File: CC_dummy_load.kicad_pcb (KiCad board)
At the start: 2 copper layers, 120 x 79.8 mm, 58 parts, among them P1 CONN_01X02, P2 12vFAN, P3 CONN_01X09, P4 LOAD, Q1 Darl_NPN, Q2 IRF540N, U1 LM324N, U2 MCP4921-E/P, U3 LM35

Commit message: redesign with much more vias to be able to make it DIY
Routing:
- net GND: track 49.2 -> 239.4 mm, vias 0 -> 4
- net VREF: track 100.1 -> 111.4 mm, vias 0 -> 2
- net Net-(ADC1-Pad2): track 53.0 -> 60.6 mm, vias 0 -> 1
- net ARDU-P08: track 36.0 -> 29.9 mm, vias 0 -> 2
- net ARDU-P07: track 26.0 -> 31.8 mm, vias 0 -> 2
- net Net-(ADC1-Pad8): track 72.4 -> 76.5 mm, vias 0 -> 2
- net ARDU-P09: track 53.6 -> 57.4 mm
- net ARDU-P11: track 43.3 -> 46.7 mm, vias 0 -> 2
- net Net-(C2-Pad1): track 18.9 -> 21.8 mm, vias 0 -> 2
- net ADC-VIN: track 69.8 -> 72.6 mm, vias 0 -> 1
- net Net-(RV2-Pad1): track 21.8 -> 23.0 mm, vias 0 -> 2
- net VCC: track 226.6 -> 227.2 mm, vias 0 -> 1
- net Net-(Q2-Pad1): track 43.1 -> 43.0 mm, vias 0 -> 1
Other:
- net class Default: via_dia 0.6 -> 1.2; via_drill 0.4 -> 0.6

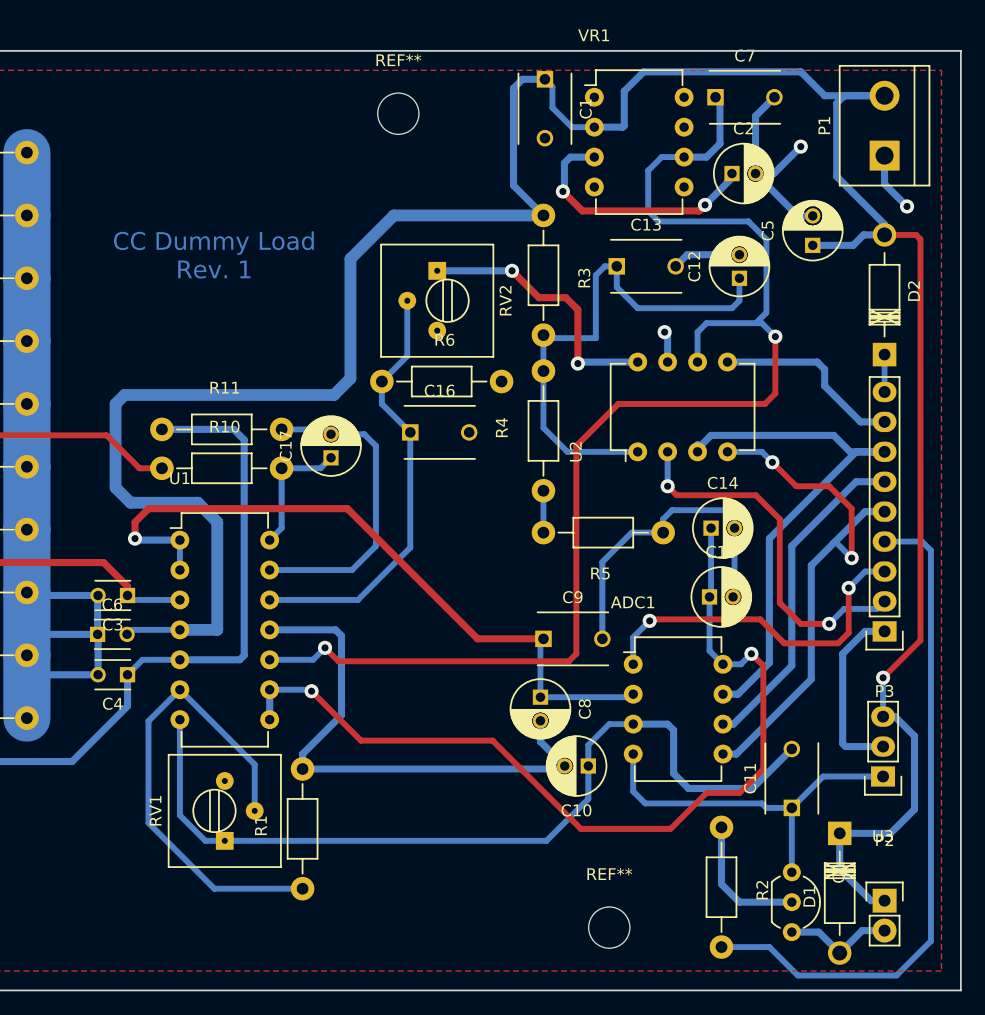
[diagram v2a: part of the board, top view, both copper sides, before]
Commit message: more coper on back face
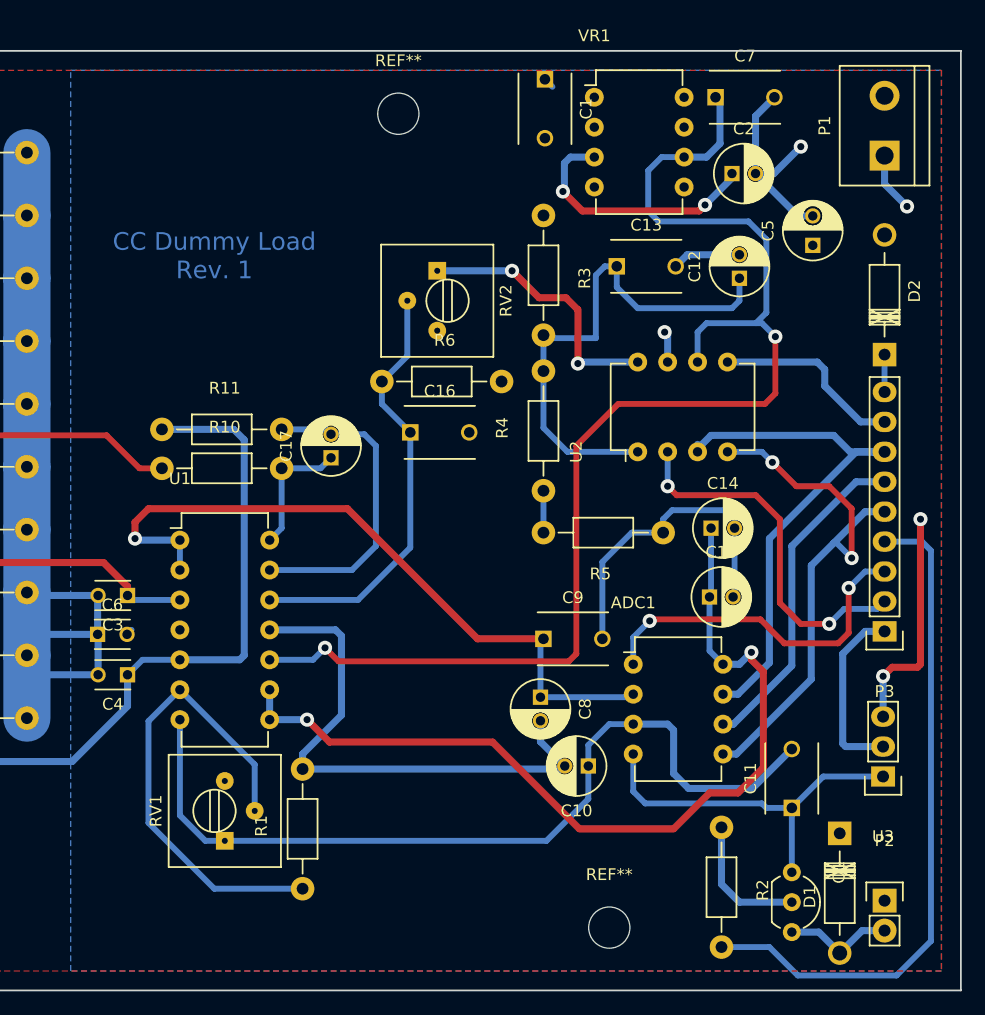
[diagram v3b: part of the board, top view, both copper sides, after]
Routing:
- net VCC: track 227.2 -> 20.8 mm, vias 1 -> 2
- net Net-(ADC1-Pad8): track 76.5 -> 75.6 mm
- added copper zone on B.Cu, net VCC
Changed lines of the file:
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@@
     (thickness 1.6)
     (drawings 6)
-    (tracks 410)
+    (tracks 365)
     (zones 0)
     (modules 58)
@@
   )
   (setup
-    (last_trace_width 0.5)
+    (last_trace_width 0.6)
     (user_trace_width 0.5)
     (user_trace_width 0.6)
@@
   (via (at 202.565 78.232) (size 1.2) (drill 0.6) (layers F.Cu B.Cu) (net 4))
   (segment (start 200.66 76.327) (end 202.565 78.232) (width 0.6) (layer B.Cu) (net 4))
-  (segment (start 182.927 83.312) (end 182.753 83.312) (width 0.5) (layer B.Cu) (net 4))
   (segment (start 187.928 111.252) (end 187.801 111.379) (width 0.5) (layer B.Cu) (net 4))
   (segment (start 173.26 125.984) (end 173.514 125.73) (width 0.6) (layer B.Cu) (net 4))
@@
   (segment (start 184.785 99.06) (end 184.785 98.425) (width 0.6) (layer B.Cu) (net 7))
   (segment (start 199.644 99.06) (end 200.66 99.06) (width 0.6) (layer B.Cu) (net 7))
-  (segment (start 148.463 119.253) (end 151.892 119.253) (width 0.5) (layer B.Cu) (net 8))
-  (segment (start 188.468 117.094) (end 186.944 117.094) (width 0.5) (layer B.Cu) (net 8))
-  (segment (start 189.357 116.205) (end 188.468 117.094) (width 0.5) (layer B.Cu) (net 8))
-  (via (at 189.357 116.205) (size 1.2) (drill 0.6) (layers F.Cu B.Cu) (net 8))
-  (segment (start 190.373 117.221) (end 189.357 116.205) (width 0.5) (layer F.Cu) (net 8))
-  (segment (start 190.373 125.984) (end 190.373 117.221) (width 0.5) (layer F.Cu) (net 8))
-  (segment (start 188.341 128.016) (end 190.373 125.984) (width 0.5) (layer F.Cu) (net 8))
-  (segment (start 185.547 128.016) (end 188.341 128.016) (width 0.5) (layer F.Cu) (net 8))
-  (segment (start 182.499 131.064) (end 185.547 128.016) (width 0.5) (layer F.Cu) (net 8))
-  (segment (start 174.879 131.064) (end 182.499 131.064) (width 0.5) (layer F.Cu) (net 8))
-  (segment (start 167.386 123.571) (end 174.879 131.064) (width 0.5) (layer F.Cu) (net 8))
-  (segment (start 156.21 123.571) (end 167.386 123.571) (width 0.5) (layer F.Cu) (net 8))
-  (segment (start 152.019 119.38) (end 156.21 123.571) (width 0.5) (layer F.Cu) (net 8))
-  (via (at 152.019 119.38) (size 1.2) (drill 0.6) (layers F.Cu B.Cu) (net 8))
-  (segment (start 151.892 119.253) (end 152.019 119.38) (width 0.5) (layer B.Cu) (net 8))
+  (segment (start 148.463 121.793) (end 151.638 121.793) (width 0.6) (layer B.Cu) (net 8))
+  (segment (start 188.341 117.094) (end 186.944 117.094) (width 0.6) (layer B.Cu) (net 8))
+  (segment (start 189.357 116.078) (end 188.341 117.094) (width 0.6) (layer B.Cu) (net 8))
+  (via (at 189.357 116.078) (size 1.2) (drill 0.6) (layers F.Cu B.Cu) (net 8))
+  (segment (start 189.357 116.713) (end 189.357 116.078) (width 0.6) (layer F.Cu) (net 8))
+  (segment (start 190.373 117.729) (end 189.357 116.713) (width 0.6) (layer F.Cu) (net 8))
+  (segment (start 190.373 125.857) (end 190.373 117.729) (width 0.6) (layer F.Cu) (net 8))
+  (segment (start 188.214 128.016) (end 190.373 125.857) (width 0.6) (layer F.Cu) (net 8))
+  (segment (start 185.801 128.016) (end 188.214 128.016) (width 0.6) (layer F.Cu) (net 8))
+  (segment (start 182.753 131.064) (end 185.801 128.016) (width 0.6) (layer F.Cu) (net 8))
+  (segment (start 174.752 131.064) (end 182.753 131.064) (width 0.6) (layer F.Cu) (net 8))
+  (segment (start 167.386 123.698) (end 174.752 131.064) (width 0.6) (layer F.Cu) (net 8))
+  (segment (start 153.543 123.698) (end 167.386 123.698) (width 0.6) (layer F.Cu) (net 8))
+  (segment (start 151.638 121.793) (end 153.543 123.698) (width 0.6) (layer F.Cu) (net 8))
+  (via (at 151.638 121.793) (size 1.2) (drill 0.6) (layers F.Cu B.Cu) (net 8))
   (segment (start 148.463 121.793) (end 148.463 119.253) (width 0.6) (layer B.Cu) (net 8))
   (segment (start 185.801 111.379) (end 185.801 115.951) (width 0.5) (layer B.Cu) (net 8))
@@
   (segment (start 185.928 105.537) (end 185.928 111.252) (width 0.5) (layer B.Cu) (net 8))
   (segment (start 185.928 111.252) (end 185.801 111.379) (width 0.5) (layer B.Cu) (net 8))
-  (segment (start 200.65746 80.645) (end 203.327 80.645) (width 0.5) (layer F.Cu) (net 9))
-  (segment (start 200.533 118.237) (end 200.533 121.539) (width 0.5) (layer B.Cu) (net 9))
-  (via (at 200.533 118.237) (size 1.2) (drill 0.6) (layers F.Cu B.Cu) (net 9))
-  (segment (start 203.708 115.062) (end 200.533 118.237) (width 0.5) (layer F.Cu) (net 9))
-  (segment (start 203.708 81.026) (end 203.708 115.062) (width 0.5) (layer F.Cu) (net 9))
-  (segment (start 203.327 80.645) (end 203.708 81.026) (width 0.5) (layer F.Cu) (net 9))
-  (segment (start 140.843 114.173) (end 144.018 114.173) (width 1) (layer B.Cu) (net 9))
-  (segment (start 159.004 78.994) (end 171.704 78.994) (width 1) (layer B.Cu) (net 9))
-  (segment (start 155.321 82.677) (end 159.004 78.994) (width 1) (layer B.Cu) (net 9))
-  (segment (start 155.321 92.837) (end 155.321 82.677) (width 1) (layer B.Cu) (net 9))
-  (segment (start 153.924 94.234) (end 155.321 92.837) (width 1) (layer B.Cu) (net 9))
-  (segment (start 136.144 94.234) (end 153.924 94.234) (width 1) (layer B.Cu) (net 9))
-  (segment (start 135.382 94.996) (end 136.144 94.234) (width 1) (layer B.Cu) (net 9))
-  (segment (start 135.382 102.108) (end 135.382 94.996) (width 1) (layer B.Cu) (net 9))
-  (segment (start 136.652 103.378) (end 135.382 102.108) (width 1) (layer B.Cu) (net 9))
-  (segment (start 142.367 103.378) (end 136.652 103.378) (width 1) (layer B.Cu) (net 9))
-  (segment (start 144.018 105.029) (end 142.367 103.378) (width 1) (layer B.Cu) (net 9))
-  (segment (start 144.018 114.173) (end 144.018 105.029) (width 1) (layer B.Cu) (net 9))
-  (segment (start 196.85254 131.445) (end 201.168 131.445) (width 0.6) (layer B.Cu) (net 9))
-  (segment (start 203.2 123.19) (end 201.549 121.539) (width 0.6) (layer B.Cu) (net 9))
-  (segment (start 203.2 129.413) (end 203.2 123.19) (width 0.6) (layer B.Cu) (net 9))
-  (segment (start 201.168 131.445) (end 203.2 129.413) (width 0.6) (layer B.Cu) (net 9))
-  (segment (start 201.549 121.539) (end 200.533 121.539) (width 0.6) (layer B.Cu) (net 9))
-  (segment (start 200.66 137.16) (end 199.517 137.16) (width 0.6) (layer B.Cu) (net 9))
-  (segment (start 196.85254 134.49554) (end 196.85254 131.445) (width 0.6) (layer B.Cu) (net 9))
-  (segment (start 199.517 137.16) (end 196.85254 134.49554) (width 0.6) (layer B.Cu) (net 9))
-  (segment (start 171.831 67.437) (end 169.926 67.437) (width 0.6) (layer B.Cu) (net 9))
-  (segment (start 169.926 67.437) (end 169.164 68.199) (width 0.6) (layer B.Cu) (net 9))
-  (segment (start 169.164 68.199) (end 169.164 76.454) (width 0.6) (layer B.Cu) (net 9))
-  (segment (start 169.164 76.454) (end 171.704 78.994) (width 0.6) (layer B.Cu) (net 9))
-  (segment (start 200.66 68.834) (end 195.58 68.834) (width 0.6) (layer B.Cu) (net 9))
-  (segment (start 178.435 71.501) (end 176.022 71.501) (width 0.6) (layer B.Cu) (net 9))
-  (segment (start 178.562 71.374) (end 178.435 71.501) (width 0.6) (layer B.Cu) (net 9))
-  (segment (start 178.562 68.453) (end 178.562 71.374) (width 0.6) (layer B.Cu) (net 9))
-  (segment (start 180.213 66.802) (end 178.562 68.453) (width 0.6) (layer B.Cu) (net 9))
-  (segment (start 193.548 66.802) (end 180.213 66.802) (width 0.6) (layer B.Cu) (net 9))
-  (segment (start 195.58 68.834) (end 193.548 66.802) (width 0.6) (layer B.Cu) (net 9))
-  (segment (start 200.65746 80.645) (end 198.882 80.645) (width 0.6) (layer B.Cu) (net 9))
-  (segment (start 197.993 81.534) (end 194.564 81.534) (width 0.6) (layer B.Cu) (net 9))
-  (segment (start 198.882 80.645) (end 197.993 81.534) (width 0.6) (layer B.Cu) (net 9))
-  (segment (start 200.65746 80.645) (end 200.65746 79.75346) (width 0.6) (layer B.Cu) (net 9))
-  (segment (start 200.65746 79.75346) (end 196.596 75.692) (width 0.6) (layer B.Cu) (net 9))
-  (segment (start 197.231 68.834) (end 200.66 68.834) (width 0.6) (layer B.Cu) (net 9))
-  (segment (start 196.596 69.469) (end 197.231 68.834) (width 0.6) (layer B.Cu) (net 9))
-  (segment (start 196.596 75.692) (end 196.596 69.469) (width 0.6) (layer B.Cu) (net 9))
-  (segment (start 200.66 137.16) (end 200.53554 137.16) (width 0.5) (layer B.Cu) (net 9))
-  (segment (start 140.843 114.173) (end 136.739 114.173) (width 0.5) (layer B.Cu) (net 9))
+  (segment (start 200.533 121.539) (end 200.533 118.11) (width 0.6) (layer B.Cu) (net 9))
+  (via (at 203.708 104.775) (size 1.2) (drill 0.6) (layers F.Cu B.Cu) (net 9))
+  (segment (start 203.708 117.094) (end 203.708 104.775) (width 0.6) (layer F.Cu) (net 9))
+  (segment (start 203.454 117.348) (end 203.708 117.094) (width 0.6) (layer F.Cu) (net 9))
+  (segment (start 201.295 117.348) (end 203.454 117.348) (width 0.6) (layer F.Cu) (net 9))
+  (segment (start 200.533 118.11) (end 201.295 117.348) (width 0.6) (layer F.Cu) (net 9))
+  (via (at 200.533 118.11) (size 1.2) (drill 0.6) (layers F.Cu B.Cu) (net 9))
   (segment (start 136.739 114.173) (end 136.358 114.554) (width 0.5) (layer B.Cu) (net 9))
-  (segment (start 176.022 71.501) (end 174.117 71.501) (width 0.5) (layer B.Cu) (net 9))
-  (segment (start 174.117 71.501) (end 172.466 69.85) (width 0.5) (layer B.Cu) (net 9))
-  (segment (start 172.466 69.85) (end 172.466 68.072) (width 0.5) (layer B.Cu) (net 9))
   (segment (start 172.466 68.072) (end 171.831 67.437) (width 0.5) (layer B.Cu) (net 9))
-  (segment (start 200.66 80.64246) (end 200.65746 80.645) (width 0.5) (layer B.Cu) (net 9))
   (segment (start 187.706 75.438) (end 187.706 75.819) (width 0.6) (layer B.Cu) (net 10))
   (segment (start 187.706 75.819) (end 185.42 78.105) (width 0.6) (layer B.Cu) (net 10))
@@
       )
     )
+  )
+  (zone (net 9) (net_name VCC) (layer B.Cu) (hatch edge 0.508)
+    (connect_pads (clearance 0.508))
+    (min_thickness 0.254)
+    (fill yes (arc_segments 16) (thermal_gap 0.508) (thermal_bridge_width 0.508))
+    (polygon
+      (pts
+        (xy 205.486 143.129) (xy 131.572 143.129) (xy 131.572 66.675) (xy 205.486 66.675) (xy 205.486 143.129)
+      )
+    )

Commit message: rev 2
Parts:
- removed REF** (x4): MountingHole_3-5mm, Mounting_Holes:MountingHole_3-5mm
- removed RV1, RV3: POT, Potentiometers:Potentiometer_Trimmer-Suntan-TSR-3386P
- removed RV2: 10k, Potentiometers:Potentiometer_Trimmer-Suntan-TSR-3386P
- added C19: 150pF, Capacitors_ThroughHole:C_Disc_D3_P2.5, F.Cu at (102.2, 64.1)
- added P5: KeyPad, Pin_Headers:Pin_Header_Straight_1x07, F.Cu at (133.9, 89.4)
- added P6: LCD_I2C, Pin_Headers:Pin_Header_Straight_1x04, F.Cu at (118.7, 127.0)
- added R21: 9.09k, Resistors_ThroughHole:Resistor_Horizontal_RM10mm, F.Cu at (77.3, 76.7)
- added R22: 9.09k, Resistors_ThroughHole:Resistor_Horizontal_RM10mm, F.Cu at (99.1, 69.2)
- added R23: 10k, Resistors_ThroughHole:Resistor_Horizontal_RM10mm, F.Cu at (60.7, 83.2)
- added R24: 22k, Resistors_ThroughHole:Resistor_Horizontal_RM10mm, F.Cu at (125.2, 98.6)
- added R25: 3.3k, Resistors_ThroughHole:Resistor_Horizontal_RM10mm, F.Cu at (125.3, 101.6)
- added R26: 22k, Resistors_ThroughHole:Resistor_Horizontal_RM10mm, F.Cu at (125.3, 104.6)
- added R27: 6.8k, Resistors_ThroughHole:Resistor_Horizontal_RM10mm, F.Cu at (125.2, 89.4)
- added R28: 6.8k, Resistors_ThroughHole:Resistor_Horizontal_RM10mm, F.Cu at (125.2, 92.3)
- added R29: 4.7k, Resistors_ThroughHole:Resistor_Horizontal_RM10mm, F.Cu at (125.2, 95.2)
- C16: value 100n -> 150pF; footprint Capacitors_ThroughHole:C_Disc_D6_P5 -> Capacitors_ThroughHole:C_Disc_D3_P2.5
- C17: value 22n -> 8.2nF
- C3, C4: value C -> 100n
- P3: value CONN_01X09 -> Arduino_Nano; footprint Pin_Headers:Pin_Header_Straight_1x09 -> arduino:Nano
- R12, R13, R14, R15, R17, R18, R19, R20, R7, R9: footprint Resistors_ThroughHole:Resistor_Horizontal_RM20mm -> Resistors_ThroughHole:Resistor_Horizontal_RM10mm
- R8: value 1k -> 2k
- moved P1 157.9 mm to (49.7, 117.6), turned to 270 degrees
- moved C5 140.9 mm to (58.5, 118.2)
- moved C11 130.1 mm to (66.2, 99.3), turned to 0 degrees
- moved C12 122.3 mm to (68.5, 108.5)
- moved R3 113.9 mm to (64.3, 121.9), turned to 0 degrees
- moved C13 113.6 mm to (68.5, 113.5)
- moved R4 111.0 mm to (64.3, 125.3), turned to 180 degrees
- moved C10 110.8 mm to (73.8, 81.8)
- moved ADC1 108.0 mm to (74.2, 92.6)
- moved C15 106.6 mm to (81.8, 88.0), turned to 90 degrees
- moved C9 102.8 mm to (71.1, 93.7), turned to 180 degrees
- moved R5 100.7 mm to (78.0, 125.3)
- moved C14 99.9 mm to (86.9, 92.5)
- moved R10 99.5 mm to (49.1, 71.8)
- moved P3 99.1 mm to (101.7, 109.0), turned to 90 degrees
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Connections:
- P3 pad 1: ARDU-A0 -> ARDU-P12
- P3 pad 2: ARDU-P07 -> ARDU-P11
- P3 pad 3: ARDU-P08 -> Net-(P3-Pad3)
- P3 pad 5: ARDU-P11 -> ARDU-P08
- P3 pad 6: ARDU-P12 -> ARDU-P07
- P3 pad 7: ARDU-P13 -> Net-(P3-Pad7)
- P3 pad 8: GND -> Net-(P3-Pad8)
- P3 pad 9: Net-(D2-Pad1) -> Net-(P3-Pad9)
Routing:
- net VCC: track 20.8 -> 290.6 mm, vias 2 -> 0
- net GND: track 239.2 -> 34.3 mm, vias 4 -> 0
- net ARDU-5v: track 0.00 -> 48.1 mm, vias 0 -> 2
- net Net-(ADC1-Pad8): track 75.6 -> 30.9 mm, vias 2 -> 0
- net Net-(C17-Pad1): track 11.1 -> 53.5 mm, vias 0 -> 1
- net Net-(R22-Pad1): track 23.0 -> 62.1 mm, vias 2 -> 1
- net ARDU-A1: track 0.00 -> 33.9 mm, vias 0 -> 1
- net Net-(Q2-Pad1): track 43.0 -> 9.06 mm, vias 1 -> 0
- net VREF: track 111.4 -> 79.2 mm
- net Net-(P5-Pad6): track 0.00 -> 31.8 mm
- net Net-(P3-Pad24): track 0.00 -> 31.5 mm
- net Net-(P5-Pad2): track 0.00 -> 28.9 mm
- net ARDU-P08: track 29.9 -> 58.1 mm
- net Net-(P3-Pad23): track 0.00 -> 27.4 mm
- net ADC-VIN: track 72.6 -> 47.3 mm, vias 1 -> 0
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- added copper zone on B.Cu, net GND
- removed copper zone on B.Cu, net VCC
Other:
- board size 120 x 79.8 mm -> 109.9 x 99.6 mm
- net class Default: clearance 0.2 -> 0.3; trace_width 0.25 -> 0.6
- rule trace_clearance: 0.2 -> 0.3
- rule trace_min: 0.2 -> 0.6
- rule via_min_size: 0.4 -> 1
- board text added: "+ Power -"
- board text added: "- Load +"
- board text added: "1 - Ardu"
- board text added: "1 - Keypad"
- board text added: "D"
- board text added: "Fucking DC Dummy Load Rev. 2"
- board text added: "G"
- board text added: "S"
- board text removed: "CC Dummy Load Rev. 1"
